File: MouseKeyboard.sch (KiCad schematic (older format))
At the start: 9 parts

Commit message: Placed Most of the componets
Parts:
- added RV? (x2): POT, symbol POT
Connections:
- net labels added: +5V, GND
- wire segments 0 -> 6
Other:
- moved on the sheet: SW?
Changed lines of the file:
@@
 L ATmega32U4 U?
 U 1 1 54DAA5C7
-P 4450 3650
-F 0 "U?" H 3550 5350 60  0000 C CNN
-F 1 "ATmega32U4" H 3800 2100 60  0000 C CNN
-F 2 "" H 5650 4750 60  0000 C CNN
-F 3 "" H 5650 4750 60  0000 C CNN
-	1    4450 3650
+P 2550 3700
+F 0 "U?" H 1650 5400 60  0000 C CNN
+F 1 "ATmega32U4" H 1900 2150 60  0000 C CNN
+F 2 "" H 3750 4800 60  0000 C CNN
+F 3 "" H 3750 4800 60  0000 C CNN
+	1    2550 3700
 	1    0    0    -1
 $EndComp
@@
 L SW_PUSH SW?
 U 1 1 54DAA625
-P 8300 1850
-F 0 "SW?" H 8450 1960 50  0000 C CNN
-F 1 "SW_PUSH" H 8300 1770 50  0000 C CNN
-F 2 "" H 8300 1850 60  0000 C CNN
-F 3 "" H 8300 1850 60  0000 C CNN
-	1    8300 1850
+P 8300 1750
+F 0 "SW?" H 8450 1860 50  0000 C CNN
+F 1 "SW_PUSH" H 8300 1670 50  0000 C CNN
+F 2 "" H 8300 1750 60  0000 C CNN
+F 3 "" H 8300 1750 60  0000 C CNN
+	1    8300 1750
 	1    0    0    -1
 $EndComp
@@
 L SPST SW?
 U 1 1 54DAA689
-P 8300 4400
-F 0 "SW?" H 8300 4500 70  0000 C CNN
-F 1 "SPST" H 8300 4300 70  0000 C CNN
-F 2 "" H 8300 4400 60  0000 C CNN
-F 3 "" H 8300 4400 60  0000 C CNN
-	1    8300 4400
+P 8100 4300
+F 0 "SW?" H 8100 4400 70  0000 C CNN
+F 1 "SPST" H 8100 4200 70  0000 C CNN
+F 2 "" H 8100 4300 60  0000 C CNN
+F 3 "" H 8100 4300 60  0000 C CNN
+	1    8100 4300
 	1    0    0    -1
 $EndComp
@@
 L SW_PUSH SW?
 U 1 1 54DAA6B1
-P 8500 1500
-F 0 "SW?" H 8650 1610 50  0000 C CNN
-F 1 "SW_PUSH" H 8500 1420 50  0000 C CNN
-F 2 "" H 8500 1500 60  0000 C CNN
-F 3 "" H 8500 1500 60  0000 C CNN
-	1    8500 1500
+P 8300 2050
+F 0 "SW?" H 8450 2160 50  0000 C CNN
+F 1 "SW_PUSH" H 8300 1970 50  0000 C CNN
+F 2 "" H 8300 2050 60  0000 C CNN
+F 3 "" H 8300 2050 60  0000 C CNN
+	1    8300 2050
 	1    0    0    -1
 $EndComp
+$Comp
+L POT RV?
+U 1 1 54DAA84B
+P 4450 5850
+F 0 "RV?" H 4450 5750 50  0000 C CNN
+F 1 "POT" H 4450 5850 50  0000 C CNN
+F 2 "" H 4450 5850 60  0000 C CNN
+F 3 "" H 4450 5850 60  0000 C CNN
+	1    4450 5850
+	1    0    0    -1
+$EndComp
+$Comp
+L POT RV?
+U 1 1 54DAA85F
+P 5600 5850
+F 0 "RV?" H 5600 5750 50  0000 C CNN
+F 1 "POT" H 5600 5850 50  0000 C CNN
+F 2 "" H 5600 5850 60  0000 C CNN
+F 3 "" H 5600 5850 60  0000 C CNN
+	1    5600 5850
+	1    0    0    -1
+$EndComp
+$Comp
+L +5V #PWR?
+U 1 1 54DAA8BA
+P 8650 1250
+F 0 "#PWR?" H 8650 1340 20  0001 C CNN
+F 1 "+5V" H 8650 1340 30  0000 C CNN
+F 2 "" H 8650 1250 60  0000 C CNN
+F 3 "" H 8650 1250 60  0000 C CNN
+	1    8650 1250
+	1    0    0    -1
+$EndComp
+$Comp
+L +5V #PWR?
+U 1 1 54DAA9EC
+P 3250 6550
+F 0 "#PWR?" H 3250 6640 20  0001 C CNN
+F 1 "+5V" H 3250 6640 30  0000 C CNN
+F 2 "" H 3250 6550 60  0000 C CNN
+F 3 "" H 3250 6550 60  0000 C CNN
+	1    3250 6550
+	0    -1   -1   0
+$EndComp
+$Comp
+L GND #PWR?
+U 1 1 54DAAA0D
+P 5850 6750
+F 0 "#PWR?" H 5850 6750 30  0001 C CNN
+F 1 "GND" H 5850 6680 30  0001 C CNN
+F 2 "" H 5850 6750 60  0000 C CNN
+F 3 "" H 5850 6750 60  0000 C CNN
+	1    5850 6750
+	1    0    0    -1
+$EndComp
+Wire Wire Line
+	3250 6550 5350 6550
+Wire Wire Line
+	4200 6550 4200 5850
+Wire Wire Line
+	5350 6550 5350 5850
+Connection ~ 4200 6550
+Wire Wire Line
+	5850 6750 5850 5850
+Wire Wire Line
+	4700 5850 4700 6400
+Wire Wire Line
+	4700 6400 5850 6400
+Connection ~ 5850 6400
 $EndSCHEMATC

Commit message: Just found out that I don't need a 32u4 microcontroller to make this work
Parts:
- removed U?: ATmega32U4, symbol ATmega32U4
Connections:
- wire segments 6 -> 15
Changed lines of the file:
@@
 $EndDescr
-$Comp
-L ATmega32U4 U?
-U 1 1 54DAA5C7
-P 2550 3700
-F 0 "U?" H 1650 5400 60  0000 C CNN
-F 1 "ATmega32U4" H 1900 2150 60  0000 C CNN
-F 2 "" H 3750 4800 60  0000 C CNN
-F 3 "" H 3750 4800 60  0000 C CNN
-	1    2550 3700
-	1    0    0    -1
-$EndComp
 $Comp
 L SW_PUSH SW?
@@
 	4700 6400 5850 6400
 Connection ~ 5850 6400
+Wire Wire Line
+	8600 1750 8650 1750
+Wire Wire Line
+	8650 1250 8650 4300
+Wire Wire Line
+	8650 2050 8600 2050
+Connection ~ 8650 1750
+Wire Wire Line
+	8650 2350 8600 2350
+Connection ~ 8650 2050
+Wire Wire Line
+	8650 2700 8600 2700
+Connection ~ 8650 2350
+Wire Wire Line
+	8650 3000 8600 3000
+Connection ~ 8650 2700
+Connection ~ 8650 3000
+Wire Wire Line
+	8650 3350 8600 3350
+Wire Wire Line
+	8650 3650 8600 3650
+Connection ~ 8650 3350
+Wire Wire Line
+	8650 4300 8600 4300
+Connection ~ 8650 3650
 $EndSCHEMATC

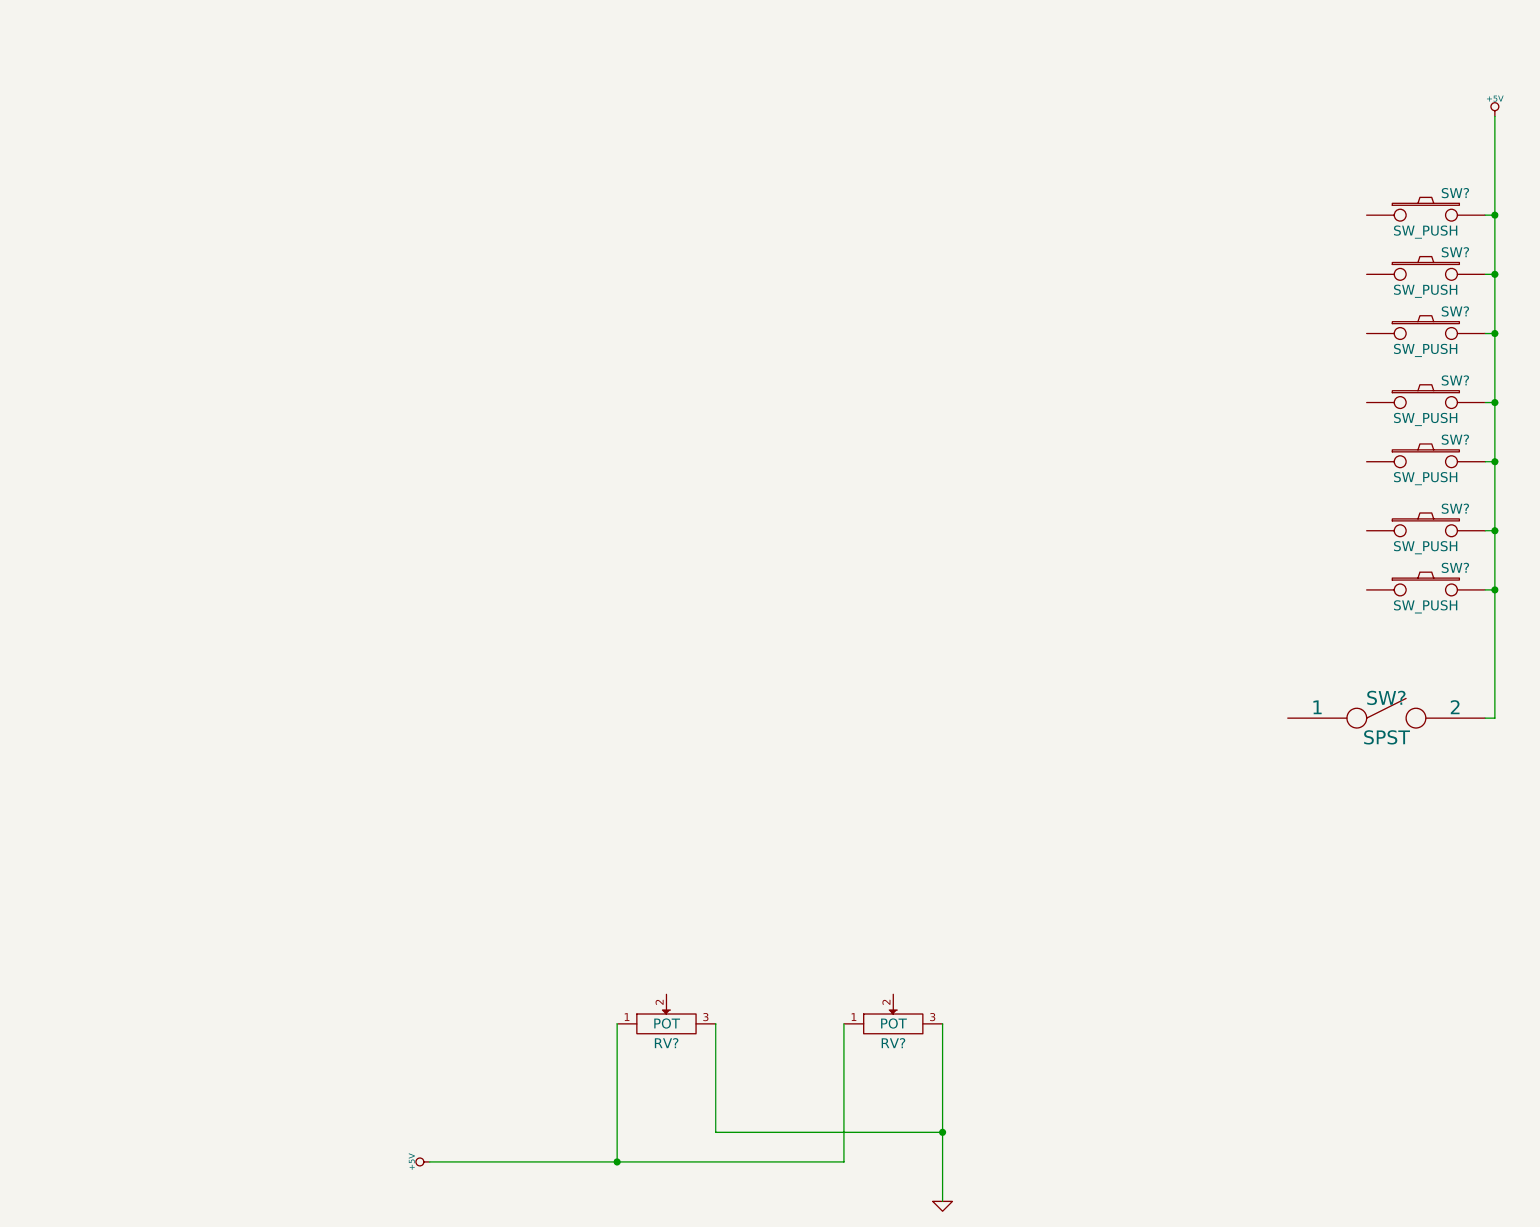
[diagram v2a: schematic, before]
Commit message: Updates
* Constants Declared
* Switched to AVR ATMega328 in schematic
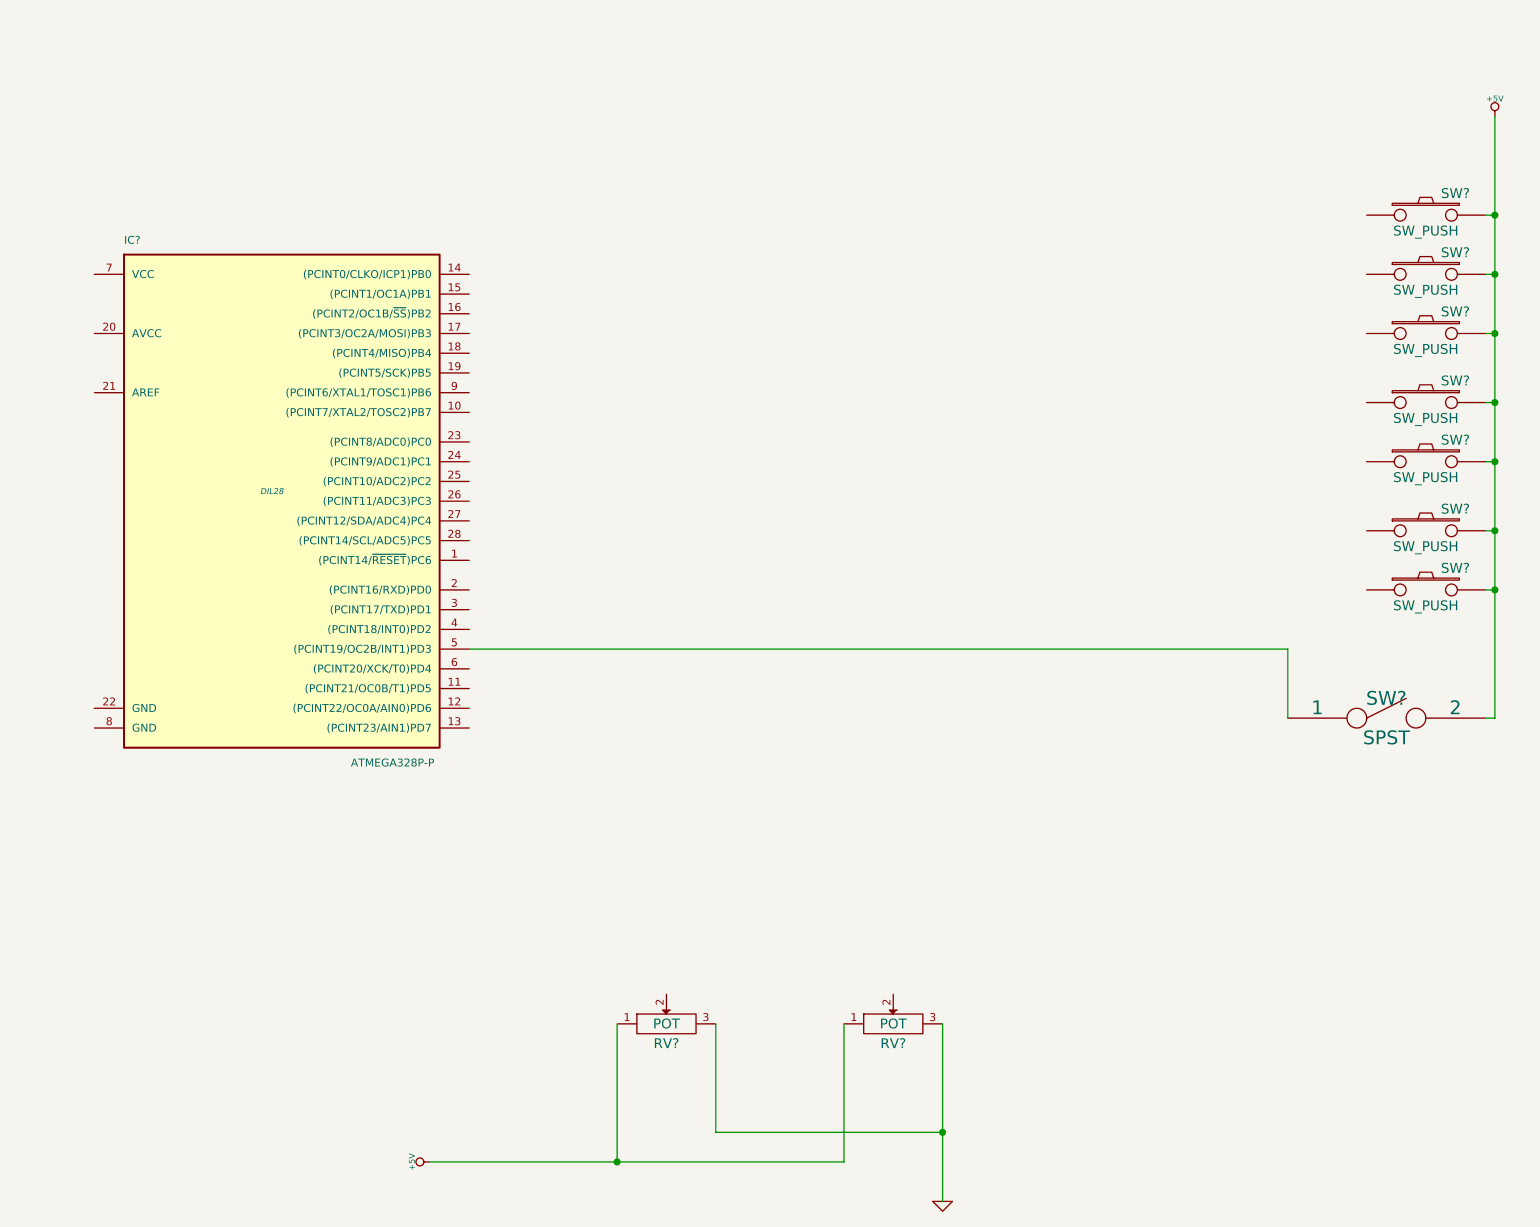
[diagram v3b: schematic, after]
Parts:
- added IC?: ATMEGA328P-P, DIL28, symbol ATMEGA328P-P
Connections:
- net at SW?.1: now also IC?.5 ((PCINT19/OC2B/INT1)PD3)
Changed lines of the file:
@@
 	8650 4300 8600 4300
 Connection ~ 8650 3650
+$Comp
+L ATMEGA328P-P IC?
+U 1 1 54DAB305
+P 2450 3150
+F 0 "IC?" H 1700 4400 40  0000 L BNN
+F 1 "ATMEGA328P-P" H 2850 1750 40  0000 L BNN
+F 2 "DIL28" H 2450 3150 30  0000 C CIN
+F 3 "" H 2450 3150 60  0000 C CNN
+	1    2450 3150
+	1    0    0    -1
+$EndComp
+Wire Wire Line
+	7600 4300 7600 3950
+Wire Wire Line
+	7600 3950 3450 3950
 $EndSCHEMATC

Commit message: Updated Schematic
Started a codeblocks project for this
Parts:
- added J?: USB, symbol USB
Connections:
- wire segments 17 -> 25
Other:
- moved on the sheet: IC?
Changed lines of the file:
@@
 LIBS:contrib
 LIBS:valves
+LIBS:MouseKeyboard-cache
 EELAYER 24 0
 EELAYER END
@@
 $EndComp
 Wire Wire Line
-	3250 6550 5350 6550
+	3250 6550 4200 6550
+Wire Wire Line
+	4200 6550 5350 6550
 Wire Wire Line
 	4200 6550 4200 5850
@@
 Connection ~ 4200 6550
 Wire Wire Line
-	5850 6750 5850 5850
+	5850 6750 5850 6400
+Wire Wire Line
+	5850 6400 5850 5850
 Wire Wire Line
 	4700 5850 4700 6400
@@
 	8600 1750 8650 1750
 Wire Wire Line
-	8650 1250 8650 4300
+	8650 1250 8650 1750
+Wire Wire Line
+	8650 1750 8650 2050
+Wire Wire Line
+	8650 2050 8650 2350
+Wire Wire Line
+	8650 2350 8650 2700
+Wire Wire Line
+	8650 2700 8650 3000
+Wire Wire Line
+	8650 3000 8650 3350
+Wire Wire Line
+	8650 3350 8650 3650
+Wire Wire Line
+	8650 3650 8650 4300
 Wire Wire Line
 	8650 2050 8600 2050
@@
 L ATMEGA328P-P IC?
 U 1 1 54DAB305
-P 2450 3150
-F 0 "IC?" H 1700 4400 40  0000 L BNN
-F 1 "ATMEGA328P-P" H 2850 1750 40  0000 L BNN
-F 2 "DIL28" H 2450 3150 30  0000 C CIN
-F 3 "" H 2450 3150 60  0000 C CNN
-	1    2450 3150
-	1    0    0    -1
-$EndComp
-Wire Wire Line
-	7600 4300 7600 3950
-Wire Wire Line
-	7600 3950 3450 3950
+P 2500 3500
+F 0 "IC?" H 1750 4750 40  0000 L BNN
+F 1 "ATMEGA328P-P" H 2900 2100 40  0000 L BNN
+F 2 "DIL28" H 2500 3500 30  0000 C CIN
+F 3 "" H 2500 3500 60  0000 C CNN
+	1    2500 3500
+	1    0    0    -1
+$EndComp
+Wire Wire Line
+	7600 4300 7650 4300
+$Comp
+L USB J?
+U 1 1 54DABFCC
+P 5450 1200
+F 0 "J?" H 5400 1600 60  0000 C CNN
+F 1 "USB" V 5200 1350 60  0000 C CNN
+F 2 "" H 5450 1200 60  0000 C CNN
+F 3 "" H 5450 1200 60  0000 C CNN
+	1    5450 1200
+	1    0    0    -1
+$EndComp
 $EndSCHEMATC

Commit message: More Wires
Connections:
- wire segments 25 -> 20
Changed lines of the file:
@@
 $EndComp
 Wire Wire Line
-	3250 6550 4200 6550
-Wire Wire Line
-	4200 6550 5350 6550
+	3250 6550 5350 6550
 Wire Wire Line
 	4200 6550 4200 5850
@@
 Connection ~ 4200 6550
 Wire Wire Line
-	5850 6750 5850 6400
-Wire Wire Line
-	5850 6400 5850 5850
+	5850 5850 5850 6750
 Wire Wire Line
 	4700 5850 4700 6400
@@
 	8600 1750 8650 1750
 Wire Wire Line
-	8650 1250 8650 1750
-Wire Wire Line
-	8650 1750 8650 2050
-Wire Wire Line
-	8650 2050 8650 2350
-Wire Wire Line
-	8650 2350 8650 2700
-Wire Wire Line
-	8650 2700 8650 3000
-Wire Wire Line
-	8650 3000 8650 3350
-Wire Wire Line
-	8650 3350 8650 3650
-Wire Wire Line
-	8650 3650 8650 4300
+	8650 1250 8650 4300
 Wire Wire Line
 	8650 2050 8600 2050
@@
 	1    0    0    -1
 $EndComp
+Wire Wire Line
+	4450 5700 4450 3250
+Wire Wire Line
+	4450 3250 3500 3250
+Wire Wire Line
+	5600 5700 5600 3350
+Wire Wire Line
+	5600 3350 3500 3350
 $EndSCHEMATC

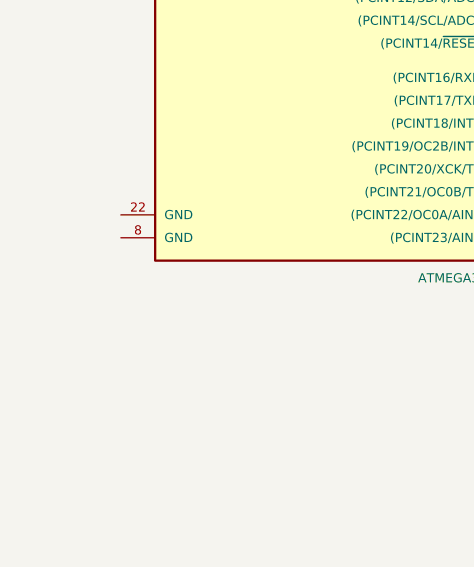
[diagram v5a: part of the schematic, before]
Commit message: New Files
* Using Adafruit's Trinket HID Combo Modded to my own needs for
controlling keyboard.
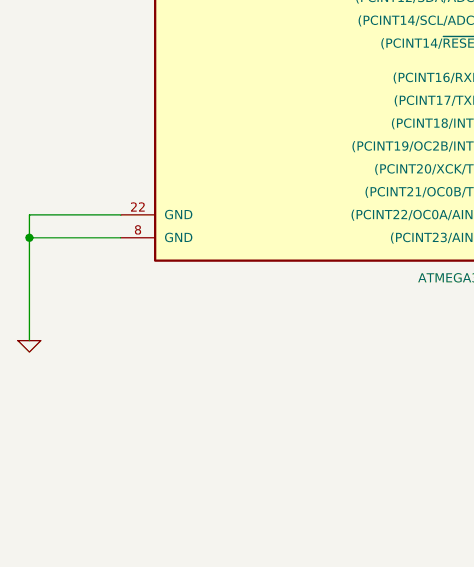
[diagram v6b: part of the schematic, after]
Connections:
- wire segments 20 -> 23
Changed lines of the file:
@@
 Wire Wire Line
 	5600 3350 3500 3350
+$Comp
+L GND #PWR?
+U 1 1 54DD39B5
+P 1200 5150
+F 0 "#PWR?" H 1200 5150 30  0001 C CNN
+F 1 "GND" H 1200 5080 30  0001 C CNN
+F 2 "" H 1200 5150 60  0000 C CNN
+F 3 "" H 1200 5150 60  0000 C CNN
+	1    1200 5150
+	1    0    0    -1
+$EndComp
+Wire Wire Line
+	1200 4600 1200 5150
+Wire Wire Line
+	1200 4700 1600 4700
+Wire Wire Line
+	1600 4600 1200 4600
+Connection ~ 1200 4700
 $EndSCHEMATC

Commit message: Stuff
* A loop for execution
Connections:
- wire segments 23 -> 24
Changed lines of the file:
@@
 	1600 4600 1200 4600
 Connection ~ 1200 4700
+$Comp
+L GND #PWR?
+U 1 1 54DD41B3
+P 4200 1550
+F 0 "#PWR?" H 4200 1550 30  0001 C CNN
+F 1 "GND" H 4200 1480 30  0001 C CNN
+F 2 "" H 4200 1550 60  0000 C CNN
+F 3 "" H 4200 1550 60  0000 C CNN
+	1    4200 1550
+	0    1    1    0
+$EndComp
+Wire Wire Line
+	5050 1550 4200 1550
 $EndSCHEMATC
